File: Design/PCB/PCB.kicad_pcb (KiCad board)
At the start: 2 copper layers, 66 parts, among them J1 SWD, J2 BLE_PROG, J3 KEYSW, J4 12V_BATT, J5 CHARGE, J6 VESC, SW1 NRST, U1 UA78M05CKVURG3, U2 TPS62162QDSGRQ1, U3 STM32F412CGU6, U4 TPS2116DRLR, U5 MCP111T-195I/LB, U6 RN4871-I/RM140, U7 TJA1051TK-3, U8 MPU-6050, Y1 NX3225SA-16.000

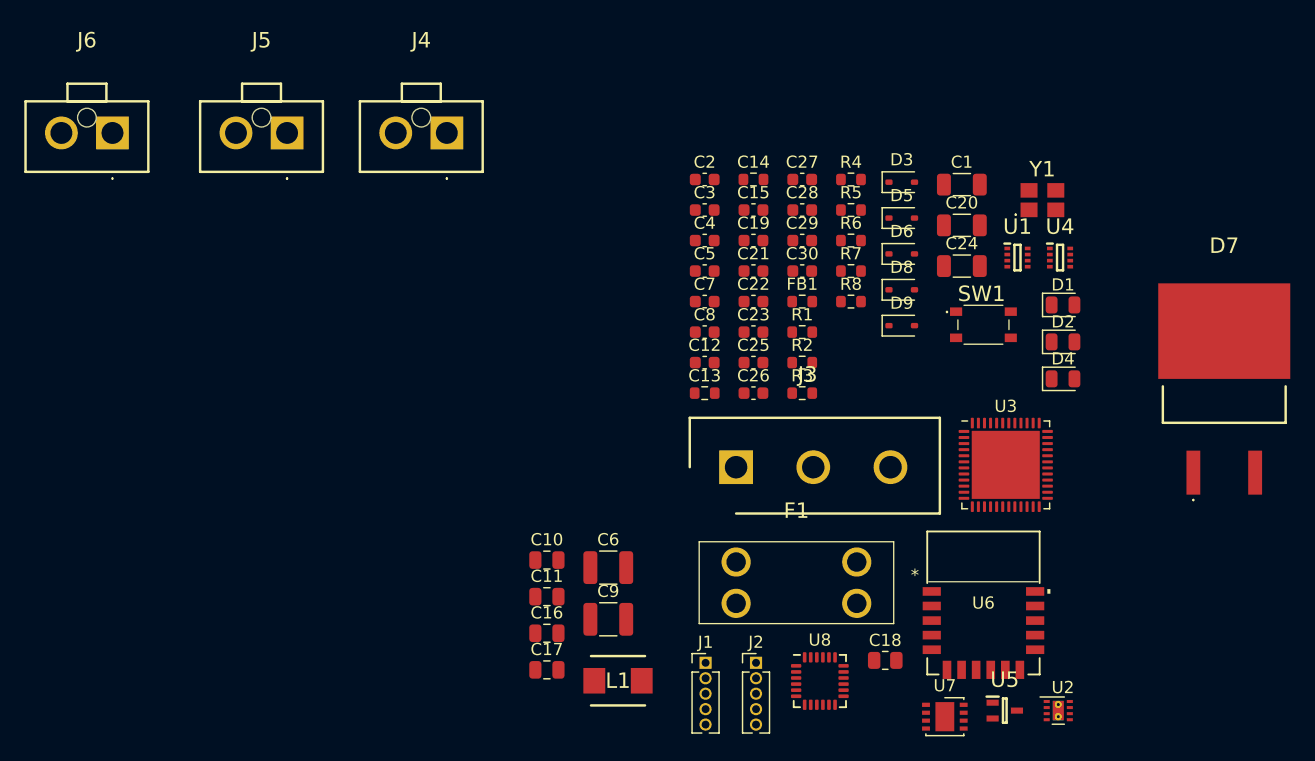
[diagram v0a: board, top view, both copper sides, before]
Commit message: Schematic formatting clean up, added TVS diode to LED PWM
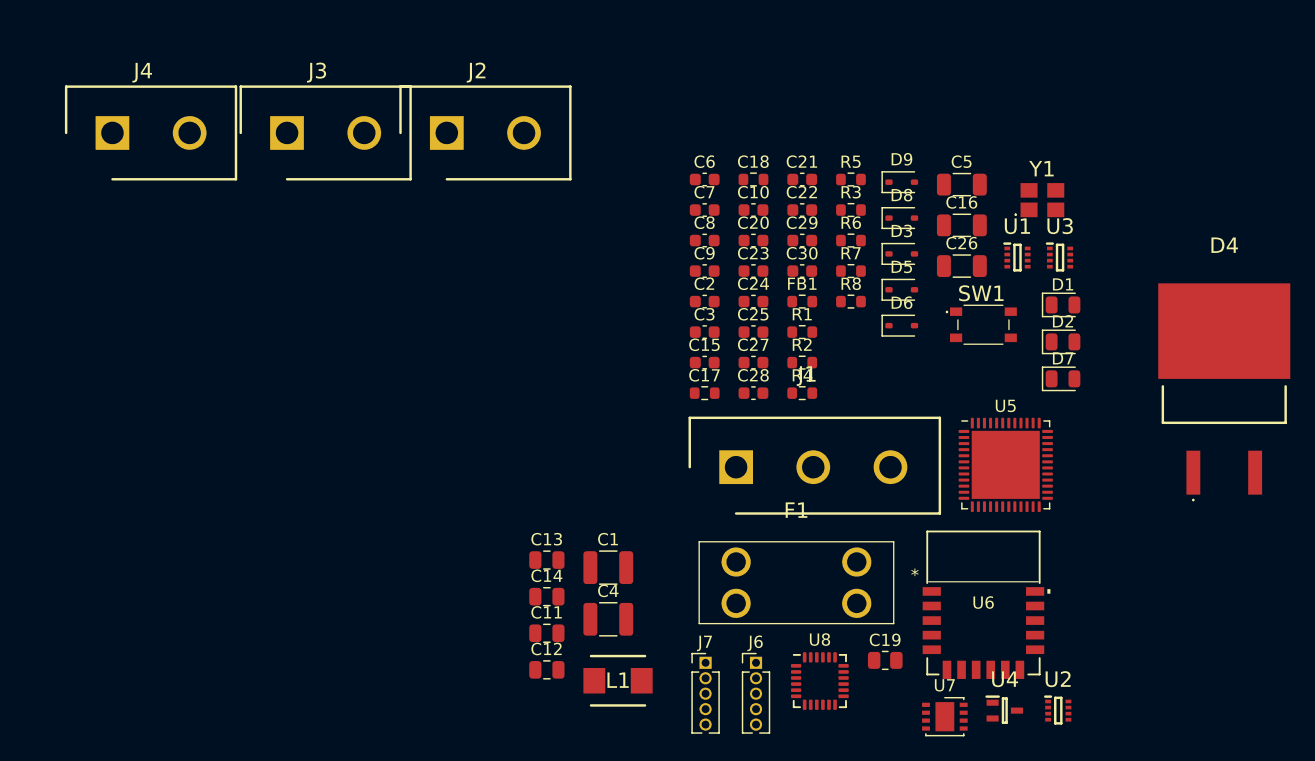
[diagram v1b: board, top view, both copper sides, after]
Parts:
- J2: renamed from J4; footprint 2159151002:2159151002 -> Molex_10-84-4020:SHDR2W166P0X635_1X2_1397X762X1397P
- J3: renamed from J5; footprint 2159151002:2159151002 -> Molex_10-84-4020:SHDR2W166P0X635_1X2_1397X762X1397P
- J4: renamed from J6; footprint 2159151002:2159151002 -> Molex_10-84-4020:SHDR2W166P0X635_1X2_1397X762X1397P
- U2: footprint Package_SON:WSON-8-1EP_2x2mm_P0.5mm_EP0.9x1.6mm_ThermalVias -> TPS2116DRLR:SOTFL50P160X60-8N
- renumbered C6 to C1, C15 to C10, C16 to C11, C17 to C12, C10 to C13, C11 to C14, C12 to C15, C20 to C16, C13 to C17, C14 to C18, C18 to C19, C7 to C2, C19 to C20, C27 to C21, C28 to C22, C21 to C23, C22 to C24, C23 to C25, C24 to C26, C25 to C27, C26 to C28, C8 to C3, C9 to C4, C1 to C5, C2 to C6, C3 to C7, C4 to C8, C5 to C9, D6 to D3, D7 to D4, D8 to D5, D9 to D6, D4 to D7, D5 to D8, D3 to D9, J3 to J1, J2 to J6, J1 to J7, R5 to R3, R3 to R4, R4 to R5, U4 to U3, U5 to U4, U3 to U5
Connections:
- U5 pad 14: /GPIO1 -> unconnected-(U5-PA4-Pad14)
- U5 pad 15: /GPIO2 -> unconnected-(U5-PA5-Pad15)
- U5 pad 16: /GPIO3 -> unconnected-(U5-PA6-Pad16)
- U5 pad 17: /GPIO4 -> unconnected-(U5-PA7-Pad17)
